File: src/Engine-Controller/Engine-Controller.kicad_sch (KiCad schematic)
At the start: 15 parts, among them J1 Jumper_NO, J2 Jumper_NO, P3 SBH11-PBPC-D10-RA-BK, U1 STM32H750VBTx

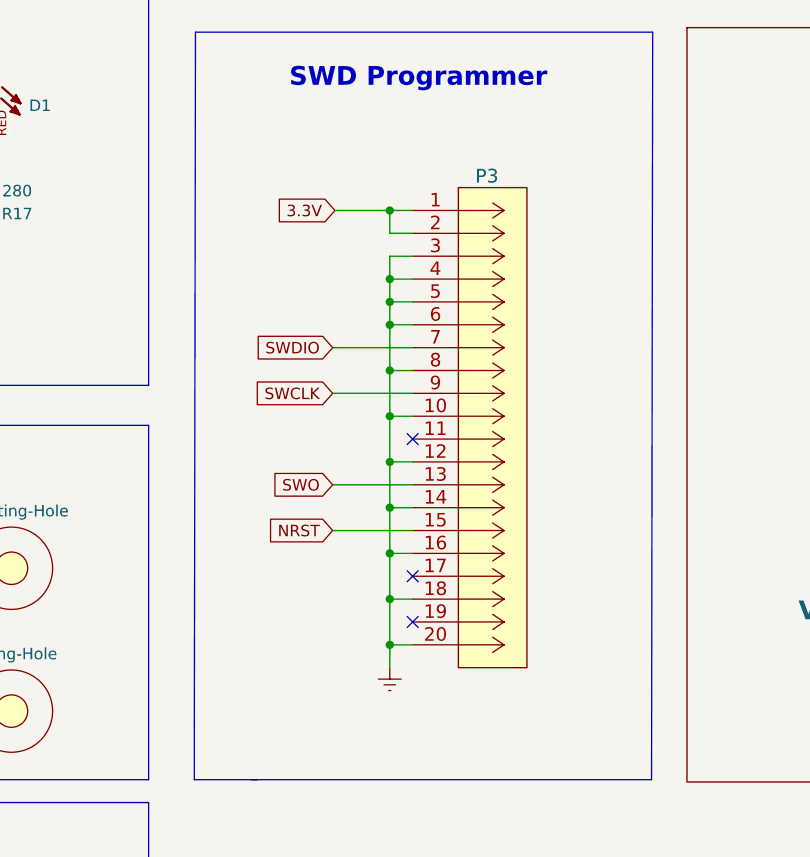
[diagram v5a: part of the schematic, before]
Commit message: Added pull up resistors to SWD signals
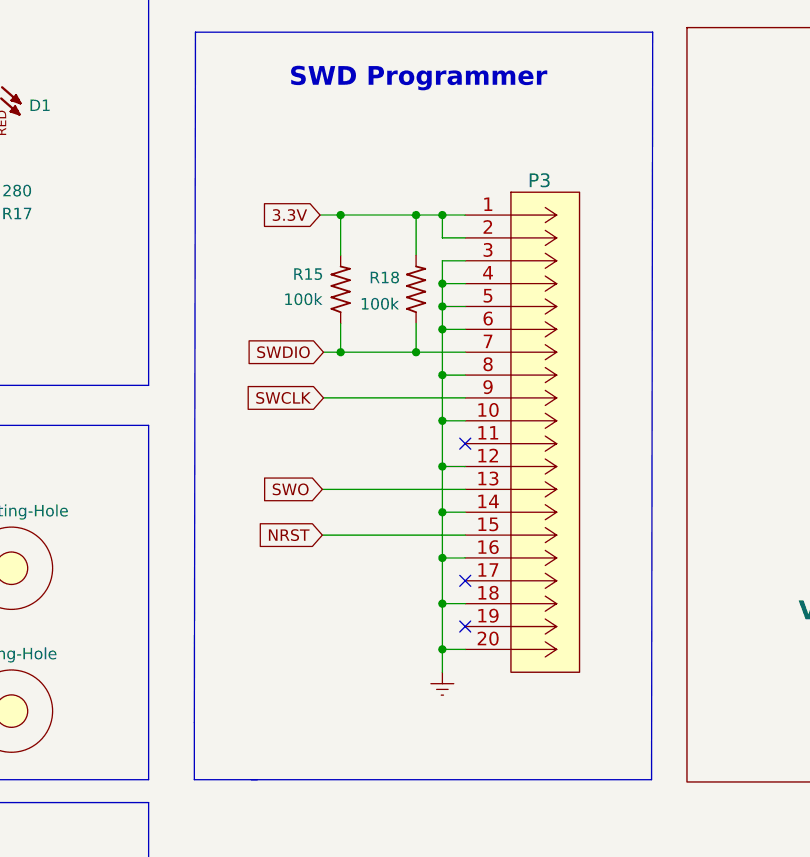
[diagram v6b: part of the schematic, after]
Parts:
- added R15, R18: 100k, symbol Engine-Controller:RES_0603
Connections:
- net 3.3V: now also R15.2, R18.2
- net SWDIO: now also R15.1, R18.1
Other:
- moved on the sheet: P3
